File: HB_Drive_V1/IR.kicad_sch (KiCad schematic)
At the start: 39 parts, among them J1 Conn_02x05_Counter_Clockwise, J3 Conn_02x03_Counter_Clockwise, J4 Conn_01x02, U1 TL082, U2 TL082, U3 TL082, U4 TL082

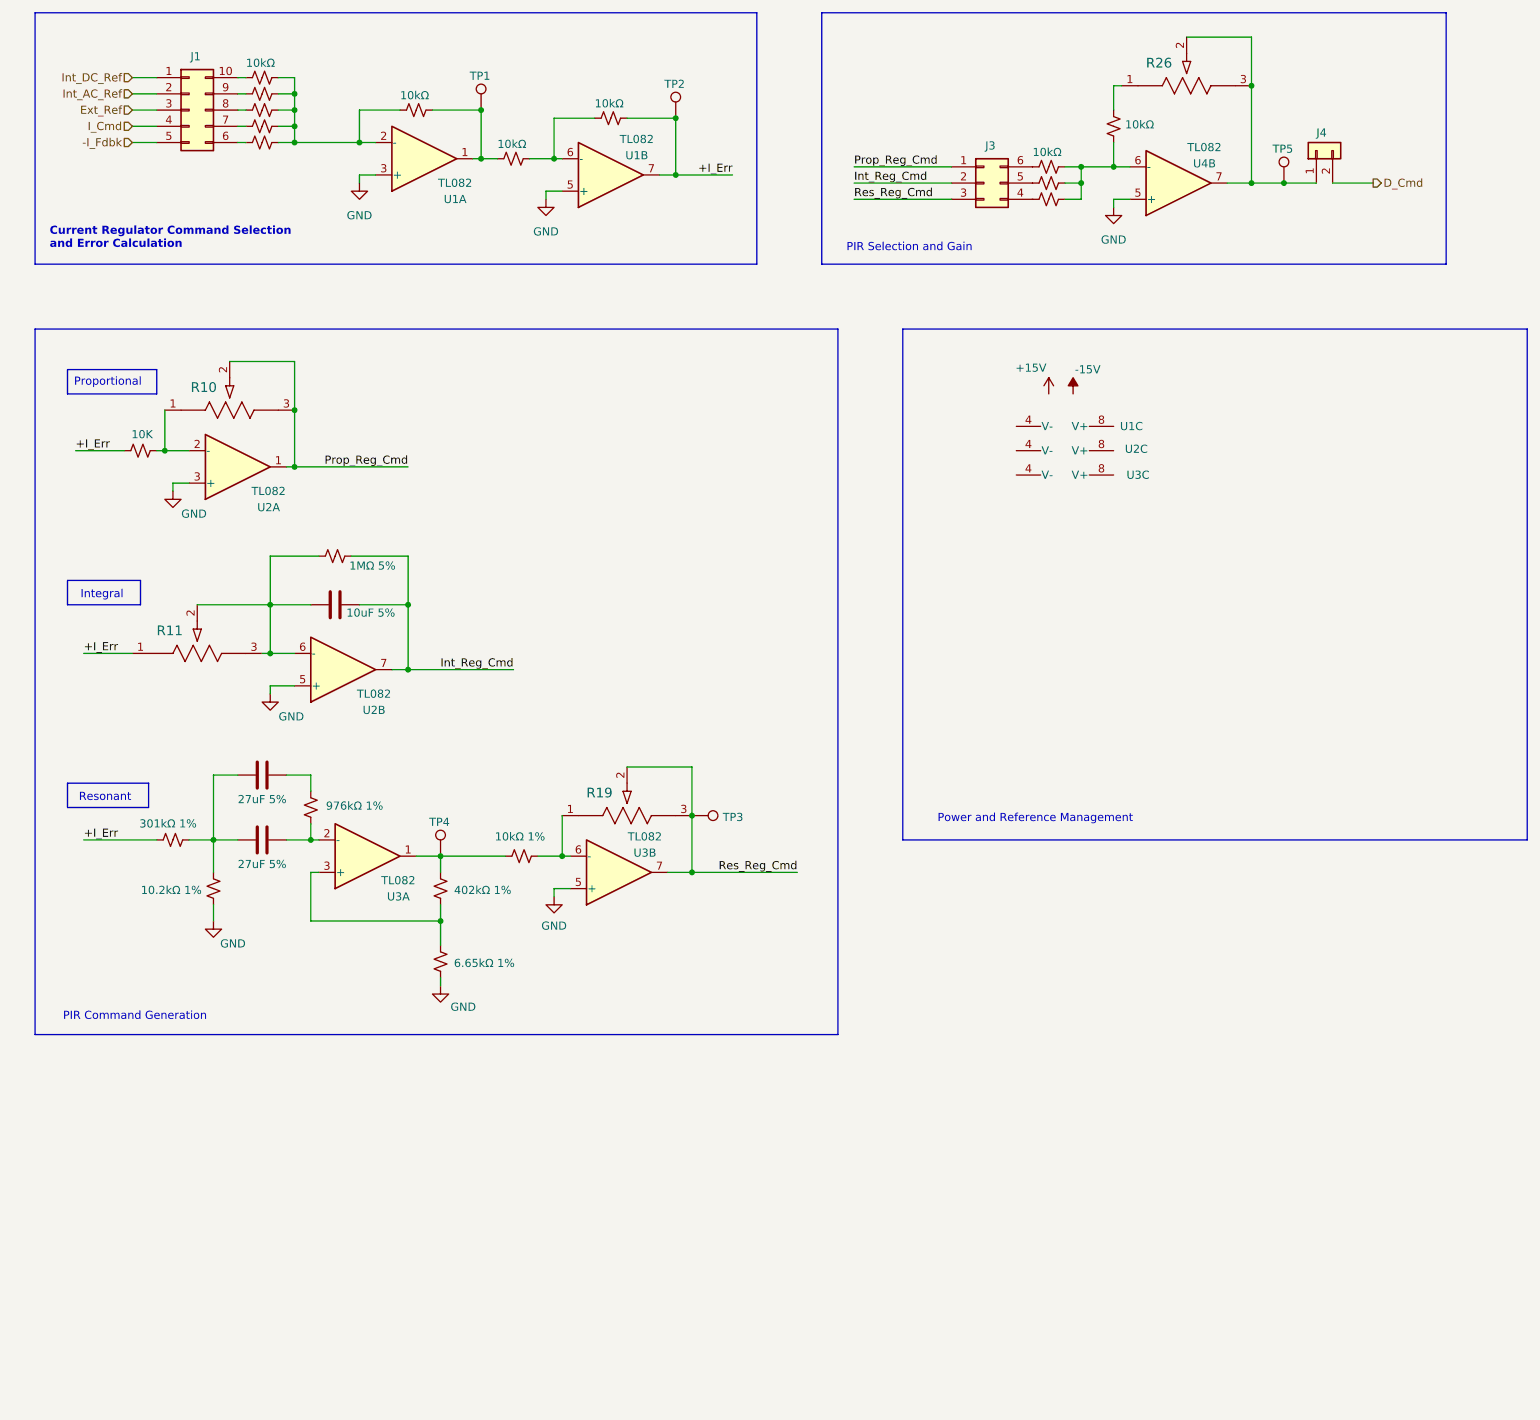
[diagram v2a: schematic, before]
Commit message: Adds Carrier Wave Circuit and Comparator Circuit
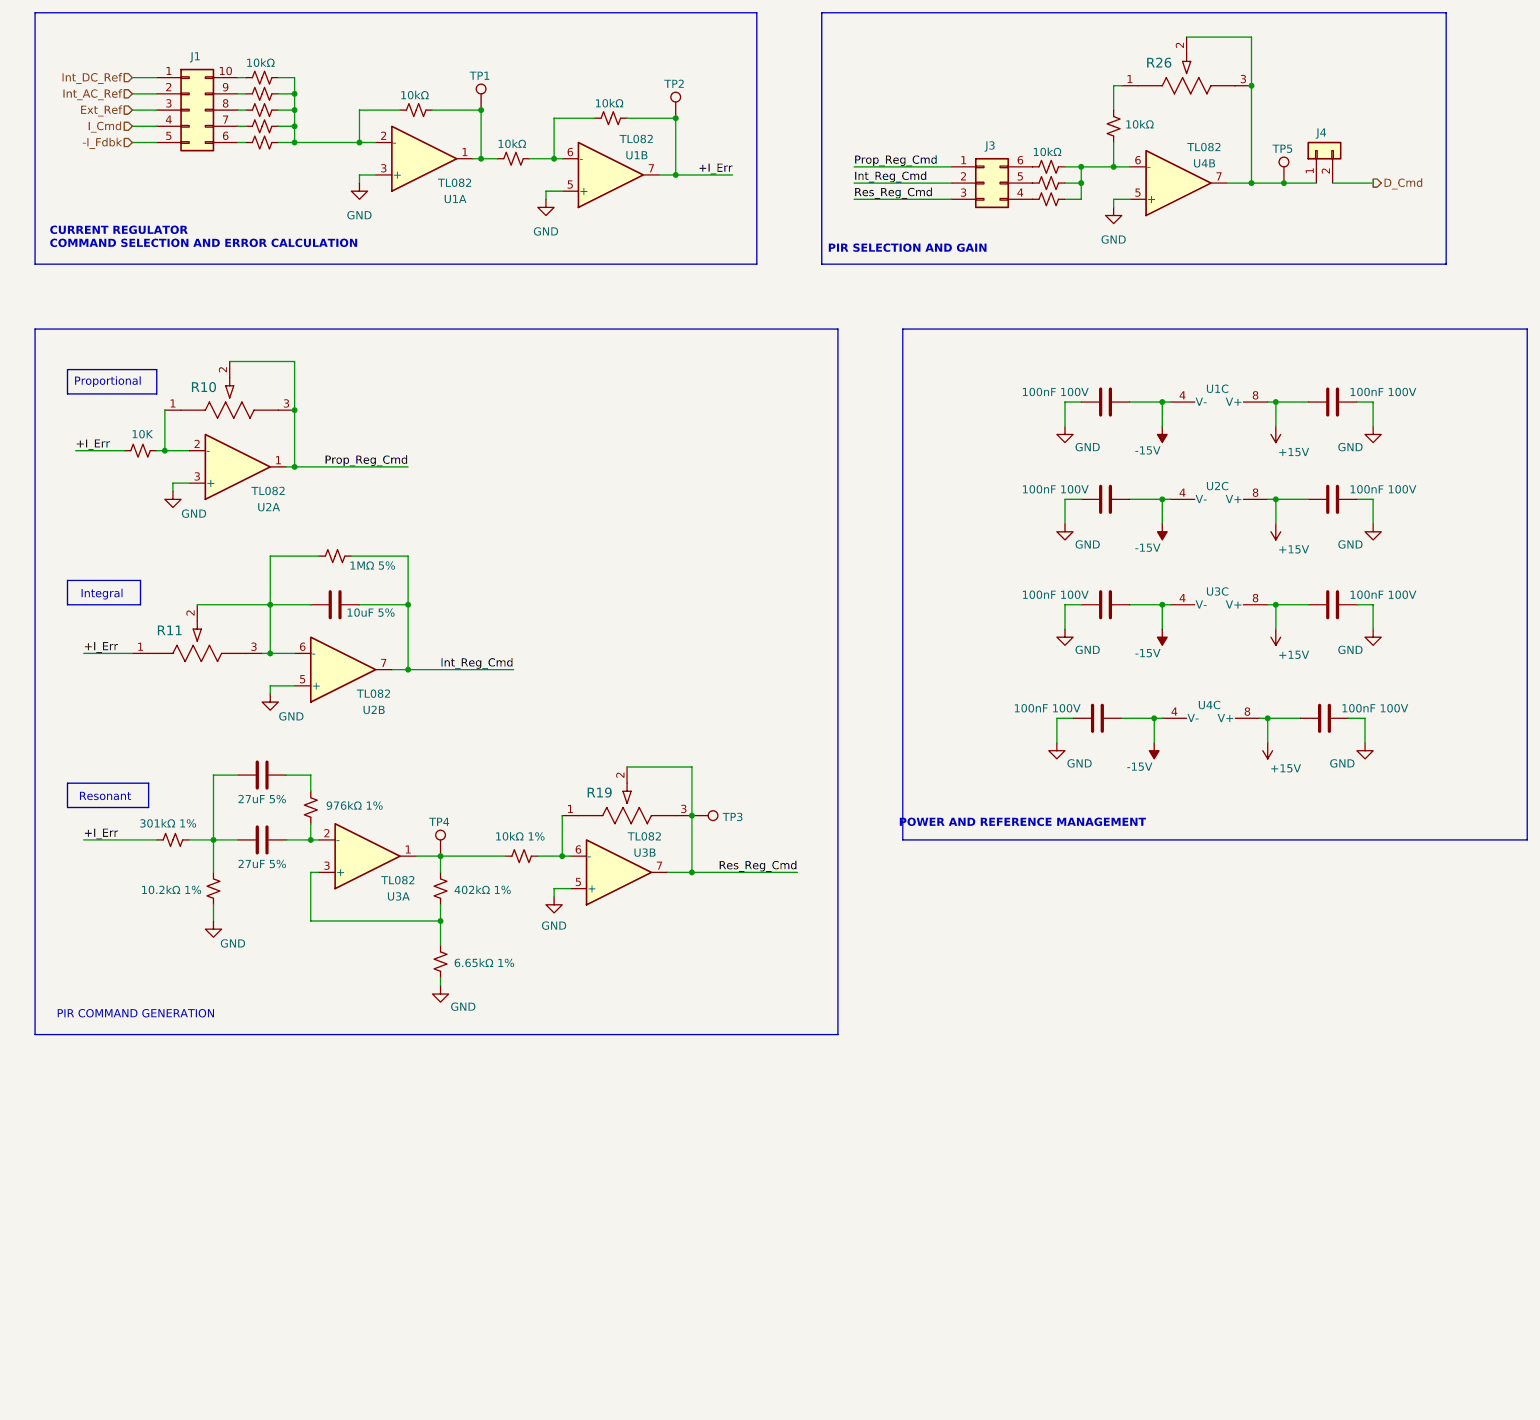
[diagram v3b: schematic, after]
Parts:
- added C10, C11, C12, C13, C14, C17, C18, C8: 100nF 100V, Capacitor_SMD:C_0603_1608Metric, symbol Device:C
- added unit 3 of U4
- U2: footprint Package_SO:SOIC-8_5.3x5.3mm_P1.27mm -> (none)
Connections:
- net +15V: now also U1.8 (V+), U2.8 (V+), U3.8 (V+), C12.2, C14.2, C18.2, C8.2, U4.8 (V+)
- net -15V: now also U1.4 (V-), U2.4 (V-), U3.4 (V-), C10.1, C11.1, C13.1, C17.1, U4.4 (V-)
- net GND: now also C10.2, C11.2, C12.1, C13.2, C14.1, C17.2, C18.1, C8.1
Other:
- note added: "CURRENT REGULATOR COMMAND SELECTION AND ERROR CALCULATION"
- note added: "PIR COMMAND GENERATION"
- note added: "PIR SELECTION AND GAIN"
- note added: "POWER AND REFERENCE MANAGEMENT"
- note removed: "Current Regulator Command Selection and Error Calculation"
- note removed: "PIR Command Generation"
- note removed: "PIR Selection and Gain"
- note removed: "Power and Reference Management"
- moved on the sheet: U1C

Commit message: Notes from conversation PF + MS
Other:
- moved on the sheet: U4C
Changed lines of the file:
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@@
 	)
 	(junction
-		(at 226.06 137.16)
+		(at 227.33 134.62)
 		(diameter 0)
 		(color 0 0 0 0)
@@
 	)
 	(junction
-		(at 208.28 137.16)
+		(at 209.55 134.62)
 		(diameter 0)
 		(color 0 0 0 0)
@@
 	(wire
 		(pts
-			(xy 226.06 140.97) (xy 226.06 137.16)
+			(xy 227.33 138.43) (xy 227.33 134.62)
 		)
 		(stroke
@@
 	(wire
 		(pts
-			(xy 208.28 137.16) (xy 209.55 137.16)
+			(xy 209.55 134.62) (xy 210.82 134.62)
 		)
 		(stroke
@@
 	(wire
 		(pts
-			(xy 203.2 137.16) (xy 208.28 137.16)
+			(xy 204.47 134.62) (xy 209.55 134.62)
 		)
 		(stroke
@@
 	(wire
 		(pts
-			(xy 193.04 140.97) (xy 193.04 137.16)
+			(xy 194.31 138.43) (xy 194.31 134.62)
 		)
 		(stroke
@@
 	(wire
 		(pts
-			(xy 193.04 137.16) (xy 195.58 137.16)
+			(xy 194.31 134.62) (xy 196.85 134.62)
 		)
 		(stroke
@@
 	(wire
 		(pts
-			(xy 241.3 137.16) (xy 238.76 137.16)
+			(xy 242.57 134.62) (xy 240.03 134.62)
 		)
 		(stroke
@@
 	(wire
 		(pts
-			(xy 241.3 140.97) (xy 241.3 137.16)
+			(xy 242.57 138.43) (xy 242.57 134.62)
 		)
 		(stroke
@@
 	(wire
 		(pts
-			(xy 231.14 137.16) (xy 226.06 137.16)
+			(xy 232.41 134.62) (xy 227.33 134.62)
 		)
 		(stroke
@@
 	(wire
 		(pts
-			(xy 208.28 140.97) (xy 208.28 137.16)
+			(xy 209.55 138.43) (xy 209.55 134.62)
 		)
 		(stroke
@@
 	(wire
 		(pts
-			(xy 226.06 137.16) (xy 224.79 137.16)
+			(xy 227.33 134.62) (xy 226.06 134.62)
 		)
 		(stroke
@@
 	(symbol
 		(lib_id "power:-15V")
-		(at 208.28 140.97 180)
+		(at 209.55 138.43 180)
 		(unit 1)
 		(body_style 1)
@@
 		(dnp no)
 		(property "Reference" "#PWR034"
-			(at 208.28 137.16 0)
+			(at 209.55 134.62 0)
 			(hide yes)
 			(show_name no)
@@
 		)
 		(property "Value" "-15V"
-			(at 205.994 144.78 0)
+			(at 207.264 142.24 0)
 			(show_name no)
 			(do_not_autoplace no)
@@
 		)
 		(property "Footprint" ""
-			(at 208.28 140.97 0)
+			(at 209.55 138.43 0)
 			(hide yes)
 			(show_name no)
@@
 		)
 		(property "Datasheet" ""
-			(at 208.28 140.97 0)
+			(at 209.55 138.43 0)
 			(hide yes)
 			(show_name no)
@@
 		)
 		(property "Description" "Power symbol creates a global label with name \"-15V\""
-			(at 208.28 140.97 0)
+			(at 209.55 138.43 0)
 			(hide yes)
 			(show_name no)
@@
 	(symbol
 		(lib_id "Amplifier_Operational:TL082")
-		(at 217.17 139.7 270)
+		(at 218.44 137.16 270)
 		(unit 3)
 		(body_style 1)
@@
 		(dnp no)
 		(property "Reference" "U4"
-			(at 216.916 135.128 90)
+			(at 218.186 132.588 90)
 			(show_name no)
 			(do_not_autoplace no)
@@
 		)
 		(property "Value" "TL082"
-			(at 217.17 134.62 90)
+			(at 218.44 132.08 90)
 			(hide yes)
 			(show_name no)
@@
 		)
 		(property "Footprint" ""
-			(at 217.17 139.7 0)
+			(at 218.44 137.16 0)
 			(hide yes)
 			(show_name no)
@@
 		)
 		(property "Datasheet" "http://www.ti.com/lit/ds/symlink/tl081.pdf"
-			(at 217.17 139.7 0)
+			(at 218.44 137.16 0)
 			(hide yes)
 			(show_name no)
@@
 		)
 		(property "Description" "Dual JFET-Input Operational Amplifiers, DIP-8/SOIC-8/SSOP-8"
-			(at 217.17 139.7 0)
+			(at 218.44 137.16 0)
 			(hide yes)
 			(show_name no)
@@
 	(symbol
 		(lib_id "Device:C")
-		(at 199.39 137.16 270)
+		(at 200.66 134.62 270)
 		(unit 1)
 		(body_style 1)
@@
 		(dnp no)
 		(property "Reference" "C17"
-			(at 201.93 135.89 90)
+			(at 203.2 133.35 90)
 			(hide yes)
 			(show_name no)
@@
 		)
 		(property "Value" "100nF 100V"
-			(at 191.516 135.636 90)
+			(at 192.786 133.096 90)
 			(show_name no)
 			(do_not_autoplace no)
@@
 		)
 		(property "Footprint" "Capacitor_SMD:C_0603_1608Metric"
-			(at 195.58 138.1252 0)
+			(at 196.85 135.5852 0)
 			(hide yes)
 			(show_name no)
@@
 		)
 		(property "Datasheet" ""
-			(at 199.39 137.16 0)
+			(at 200.66 134.62 0)
 			(hide yes)
 			(show_name no)
@@
 		)
 		(property "Description" "Unpolarized capacitor"
-			(at 199.39 137.16 0)
+			(at 200.66 134.62 0)
 			(hide yes)
 			(show_name no)
@@
 	(symbol
 		(lib_id "power:+15V")
-		(at 226.06 140.97 180)
+		(at 227.33 138.43 180)
 		(unit 1)
 		(body_style 1)
@@
 		(dnp no)
 		(property "Reference" "#PWR036"
-			(at 226.06 137.16 0)
+			(at 227.33 134.62 0)
 			(hide yes)
 			(show_name no)
@@
 		)
 		(property "Value" "+15V"
-			(at 228.854 145.034 0)
+			(at 230.124 142.494 0)
 			(show_name no)
 			(do_not_autoplace no)
@@
 		)
 		(property "Footprint" ""
-			(at 226.06 140.97 0)
+			(at 227.33 138.43 0)
 			(hide yes)
 			(show_name no)
@@
 		)
 		(property "Datasheet" ""
-			(at 226.06 140.97 0)
+			(at 227.33 138.43 0)
 			(hide yes)
 			(show_name no)
@@
 		)
 		(property "Description" "Power symbol creates a global label with name \"+15V\""
-			(at 226.06 140.97 0)
+			(at 227.33 138.43 0)
 			(hide yes)
 			(show_name no)
@@
 	(symbol
 		(lib_id "Device:C")
-		(at 234.95 137.16 270)
+		(at 236.22 134.62 270)
 		(unit 1)
 		(body_style 1)
@@
 		(dnp no)
 		(property "Reference" "C18"
-			(at 237.49 135.89 90)
+			(at 238.76 133.35 90)
 			(hide yes)
 			(show_name no)
@@
 		)
 		(property "Value" "100nF 100V"
-			(at 242.824 135.636 90)
+			(at 244.094 133.096 90)
 			(show_name no)
 			(do_not_autoplace no)
@@
 		)
 		(property "Footprint" "Capacitor_SMD:C_0603_1608Metric"
-			(at 231.14 138.1252 0)
+			(at 232.41 135.5852 0)
 			(hide yes)
 			(show_name no)
@@
 		)
 		(property "Datasheet" ""
-			(at 234.95 137.16 0)
+			(at 236.22 134.62 0)
 			(hide yes)
 			(show_name no)
@@
 		)
 		(property "Description" "Unpolarized capacitor"
-			(at 234.95 137.16 0)
+			(at 236.22 134.62 0)
 			(hide yes)
 			(show_name no)
@@
 	(symbol
 		(lib_id "power:GND")
-		(at 193.04 140.97 0)
+		(at 194.31 138.43 0)
 		(unit 1)
 		(body_style 1)
@@
 		(dnp no)
 		(property "Reference" "#PWR033"
-			(at 193.04 147.32 0)
+			(at 194.31 144.78 0)
 			(hide yes)
 			(show_name no)
@@
 		)
 		(property "Value" "GND"
-			(at 196.596 144.272 0)
+			(at 197.866 141.732 0)
 			(show_name no)
 			(do_not_autoplace no)
@@
 		)
 		(property "Footprint" ""
-			(at 193.04 140.97 0)
+			(at 194.31 138.43 0)
 			(hide yes)
 			(show_name no)
@@
 		)
 		(property "Datasheet" ""
-			(at 193.04 140.97 0)
+			(at 194.31 138.43 0)
 			(hide yes)
 			(show_name no)
@@
 		)
 		(property "Description" "Power symbol creates a global label with name \"GND\" , ground"
-			(at 193.04 140.97 0)
+			(at 194.31 138.43 0)
 			(hide yes)
 			(show_name no)
@@
 	(symbol
 		(lib_id "power:GND")
-		(at 241.3 140.97 0)
+		(at 242.57 138.43 0)
 		(mirror y)
 		(unit 1)
@@
 		(dnp no)
 		(property "Reference" "#PWR037"
-			(at 241.3 147.32 0)
+			(at 242.57 144.78 0)
 			(hide yes)
 			(show_name no)
@@
 		)
 		(property "Value" "GND"
-			(at 237.744 144.272 0)
+			(at 239.014 141.732 0)
 			(show_name no)
 			(do_not_autoplace no)
@@
 		)
 		(property "Footprint" ""
-			(at 241.3 140.97 0)
+			(at 242.57 138.43 0)
 			(hide yes)
 			(show_name no)
@@
 		)
 		(property "Datasheet" ""
-			(at 241.3 140.97 0)
+			(at 242.57 138.43 0)
 			(hide yes)
 			(show_name no)
@@
 		)
 		(property "Description" "Power symbol creates a global label with name \"GND\" , ground"
-			(at 241.3 140.97 0)
+			(at 242.57 138.43 0)
 			(hide yes)
 			(show_name no)

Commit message: adds 10v reference and DC offsets / gain control to I_fdbk and V_fdbk
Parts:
- removed R2, R3, R4, R5: 10K, Resistor_SMD:R_0603_1608Metric_Pad0.98x0.95mm_HandSolder, symbol Device:R_Small_US
- removed R20: 10kΩ, Resistor_SMD:R_0603_1608Metric_Pad0.98x0.95mm_HandSolder, symbol Device:R_Small_US
- added R10, R7, R8, R9: 10K, Resistor_SMD:R_0603_1608Metric_Pad0.98x0.95mm_HandSolder, symbol Device:R_Small_US
- added R6: 10kΩ, Resistor_SMD:R_0603_1608Metric_Pad0.98x0.95mm_HandSolder, symbol Device:R_Small_US
- added R73, R81: PV36W104C01B00, PV36W104C01B00:POT_PV36W_BRN, symbol PV36W104C01B00:PV36W104C01B00
- added R74, R78, R80: 51KΩ, Resistor_SMD:R_0603_1608Metric_Pad0.98x0.95mm_HandSolder, symbol Device:R_Small_US
- added R79: 10KΩ, Resistor_SMD:R_0603_1608Metric_Pad0.98x0.95mm_HandSolder, symbol Device:R_Small_US
- added TP21: TestPoint, TestPoint:TestPoint_Loop_D2.60mm_Drill1.6mm_Beaded, symbol Connector:TestPoint
- added U13: TL082, Package_SO:SOIC-8_5.3x5.3mm_P1.27mm, symbol Amplifier_Operational:TL082
- J3: renamed from J4; footprint (none) -> Connector_PinHeader_1.27mm:PinHeader_1x02_P1.27mm_Vertical
- U4: footprint (none) -> Package_SO:SOIC-8_5.3x5.3mm_P1.27mm
- renumbered C2 to C1, C14 to C10, C18 to C11, C3 to C2, C1 to C3, C10 to C4, C11 to C5, C13 to C6, C17 to C7, C12 to C9, J3 to J2, R11 to R1, R13 to R11, R21 to R13, R16 to R14, R17 to R15, R22 to R16, R18 to R17, R19 to R18, R23 to R19, R9 to R2, R24 to R20, R6 to R21, R7 to R22, R25 to R23, R26 to R24, R10 to R3, R14 to R4, R15 to R5, TP4 to TP1, TP1 to TP2, TP2 to TP3, TP3 to TP4, U2 to U1, U3 to U2, U1 to U3
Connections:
- net +15V: now also R73.1
- net GND: now also R79.1, R80.2
- net at J1.10 (Pin_10): now also R6.2
- net at J1.6 (Pin_6): now also R10.1
- net at J1.7 (Pin_7): now also R9.1
- net at J1.8 (Pin_8): now also R8.1
- net at J1.9 (Pin_9): now also R7.1
- net Err_Cmd: now reaches R13.2, U3.2 (-)
- net Err_Cmd: now also R81.1, TP21.1, U13.7
- new net: R80.1, R81.2, R81.3, U13.6 (-)
- new net: R74.1, R78.1, R79.2, U13.5 (+)
- new net: R73.2, R73.3, R78.2
- new net: R10.2, R6.1, R7.2, R74.2, R8.2, R9.2
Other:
- note added: "COMMAND SELECTION, DC OFFSET, AND GAIN ADJUST"
- note added: "CURRENT REGULATOR ERROR CALCULATION"
- note added: "DC Offset [0 to -15V DC]"
- note added: "Gain Adjustment"
- note removed: "CURRENT REGULATOR COMMAND SELECTION AND ERROR CALCULATION"
- moved on the sheet: J2, J3, R24, TP2, TP3, TP5, U3A, U3B, U4B
